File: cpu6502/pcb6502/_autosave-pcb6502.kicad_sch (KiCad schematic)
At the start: 38 parts, among them J1 Power, J2 RS232, J3 VIA PA, J4 VIA PB, J5 Ext RST, J6 Address, J7 Data, J8 CPU, J9 Interrupt Enable, SW1 Reset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

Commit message: Finalizing pcb
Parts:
- J8: footprint (none) -> Connector_PinHeader_2.54mm:PinHeader_2x04_P2.54mm_Vertical
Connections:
- net NMI: no longer J8.7 (Pin_7)
- no-connect marks 25 -> 26
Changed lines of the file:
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@@
   (no_connect (at 238.76 54.61))
   (no_connect (at 259.08 83.82))
+  (no_connect (at 259.08 33.02))
   (no_connect (at 257.81 128.27))
   (no_connect (at 73.66 137.16))
@@
     (stroke (width 0) (type default))
   )
-  (wire (pts (xy 254 33.02) (xy 259.08 33.02))
-    (stroke (width 0) (type default))
-  )
   (wire (pts (xy 104.14 55.88) (xy 101.6 55.88))
     (stroke (width 0) (type default))
@@
   )
   (label "R{slash}W" (at 213.36 62.23 0) (fields_autoplaced)
-    (effects (font (size 1.27 1.27)) (justify left bottom))
-  )
-  (label "NMI" (at 254 33.02 0) (fields_autoplaced)
     (effects (font (size 1.27 1.27)) (justify left bottom))
   )
@@
       (effects (font (size 1.27 1.27)))
     )
-    (property "Footprint" "" (at 264.16 27.94 0)
+    (property "Footprint" "Connector_PinHeader_2.54mm:PinHeader_2x04_P2.54mm_Vertical" (at 264.16 27.94 0)
       (effects (font (size 1.27 1.27)) hide)
     )

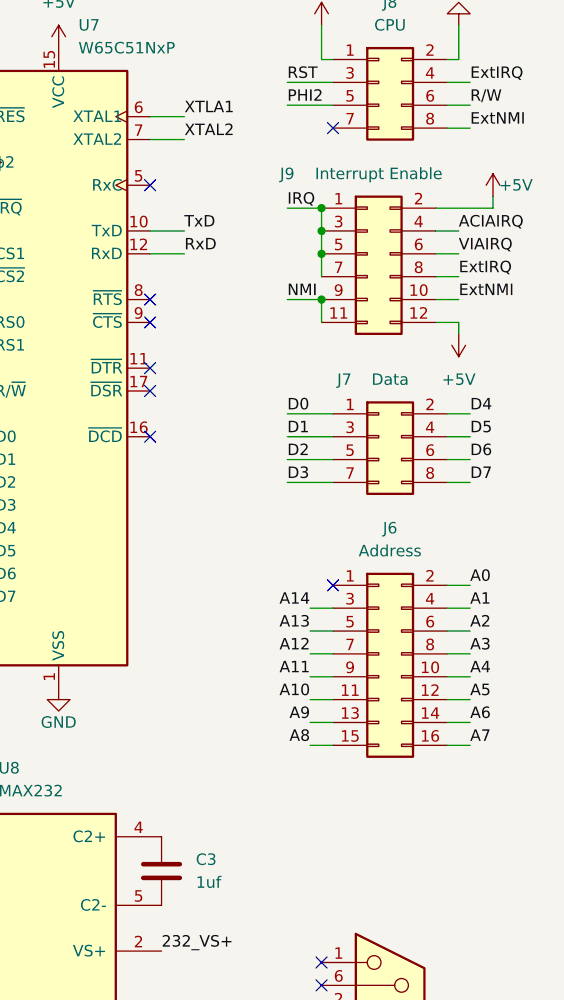
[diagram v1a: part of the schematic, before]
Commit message: add dip switches to pcb, testing rs232 programs
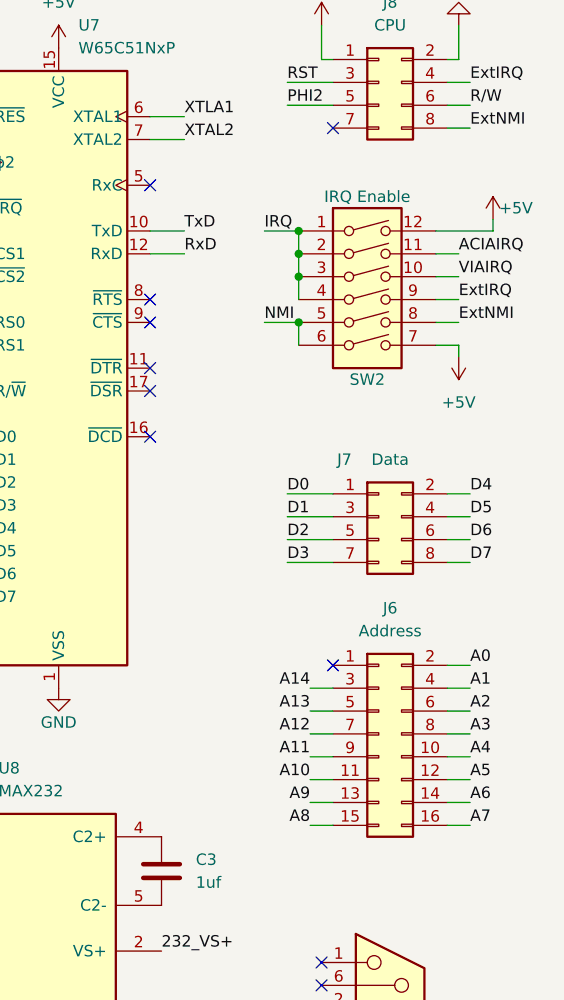
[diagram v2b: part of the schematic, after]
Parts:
- removed J9: Interrupt Enable, Connector_PinHeader_2.54mm:PinHeader_2x06_P2.54mm_Vertical, symbol Connector_Generic:Conn_02x06_Odd_Even
- added SW2: IRQ Enable, Button_Switch_THT:SW_DIP_SPSTx06_Slide_6.7x16.8mm_W7.62mm_P2.54mm_LowProfile, symbol Switch:SW_DIP_x06
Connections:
- net +5V: now also SW2.12, SW2.7
- net ACIAIRQ: now also SW2.11
- net ExtIRQ: now also SW2.9
- net ExtNMI: now also SW2.8
- net IRQ: now also SW2.1, SW2.2, SW2.3, SW2.4
- net NMI: now also SW2.5, SW2.6
- net VIAIRQ: now also SW2.10
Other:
- moved on the sheet: J6, J7
